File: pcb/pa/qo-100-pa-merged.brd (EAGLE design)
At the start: 80 x 40 mm, 1 part

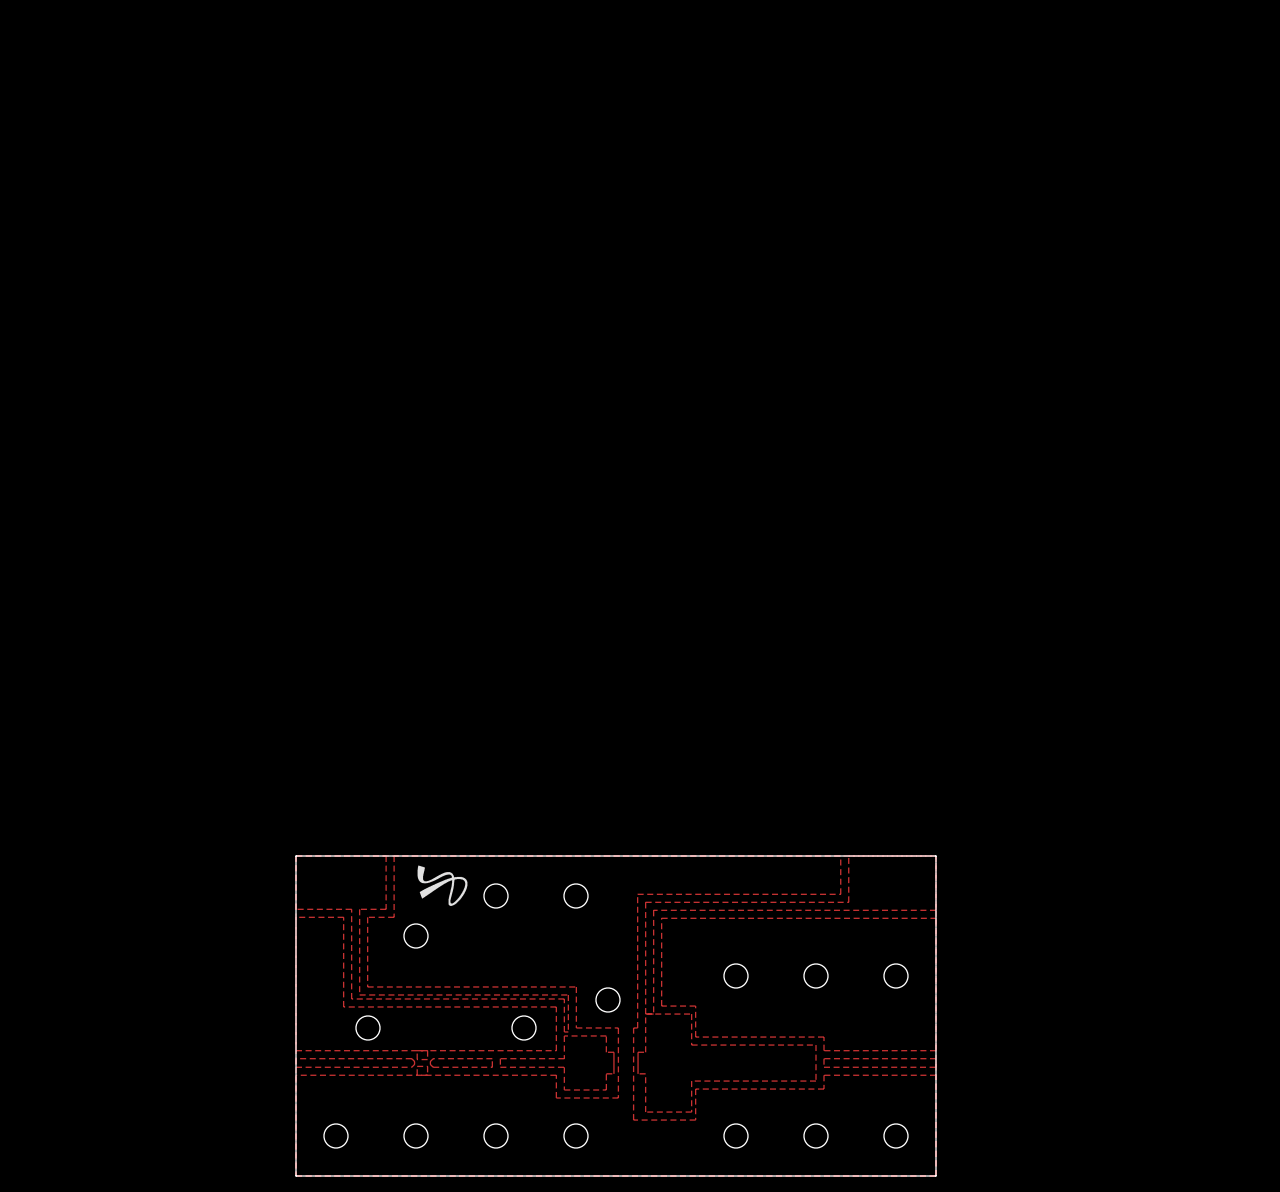
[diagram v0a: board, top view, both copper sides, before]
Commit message: Changes to PA PCBs for easier etching
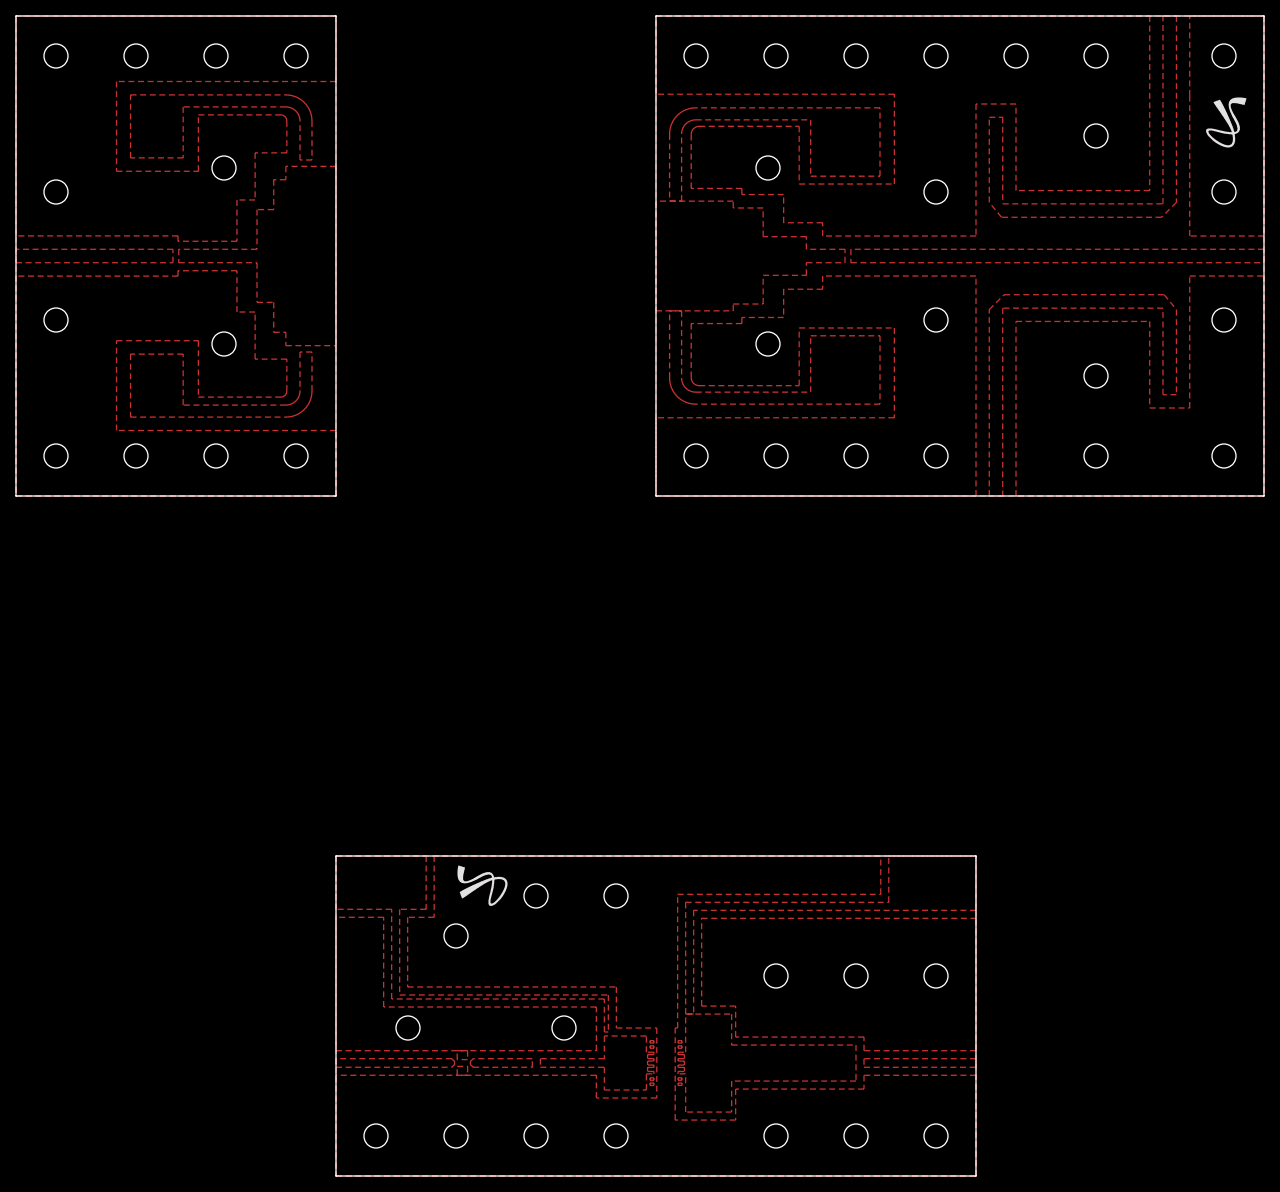
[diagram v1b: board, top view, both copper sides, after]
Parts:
- added E$2: (no value), Silkscreen:JS_5MM
- moved E$1 5.00 mm to (20.0, 39.0)
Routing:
- added copper zone on layer 1, net BIAS
- added copper zone on layer 1, net BIAS3
- added copper zone on layer 1, net BIAS4
- added copper zone on layer 1, net DRAIN
- added copper zone on layer 1, net FWD
- added copper zone on layer 1, net FWD1
- added copper zone on layer 1, net GATE2
- added copper zone on layer 1, net GND1
- added copper zone on layer 1, net GND2
- added copper zone on layer 1, net IN3
- added copper zone on layer 1, net IN4
- added copper zone on layer 1, net NEGATIVE1
- added copper zone on layer 1, net PAD
- added copper zone on layer 1, net PAD1
- added copper zone on layer 1, net PAD2
- added copper zone on layer 1, net PAD3
- added copper zone on layer 1, net PAD4
- added copper zone on layer 1, net PAD5
- added copper zone on layer 1, net PAD6
- added copper zone on layer 1, net PAD7
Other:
- board size 80 x 40 mm -> 156 x 145 mm
